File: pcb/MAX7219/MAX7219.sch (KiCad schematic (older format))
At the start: 17 parts, among them J1 Conn_01x02, J2 Conn_01x08, J3 Conn_01x06, SW1 SW_SPST, SW2 SW_SPST, SW3 SW_SPST, SW4 SW_SPST, SW5 SW_SPST, SW6 SW_SPST, SW7 SW_SPST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

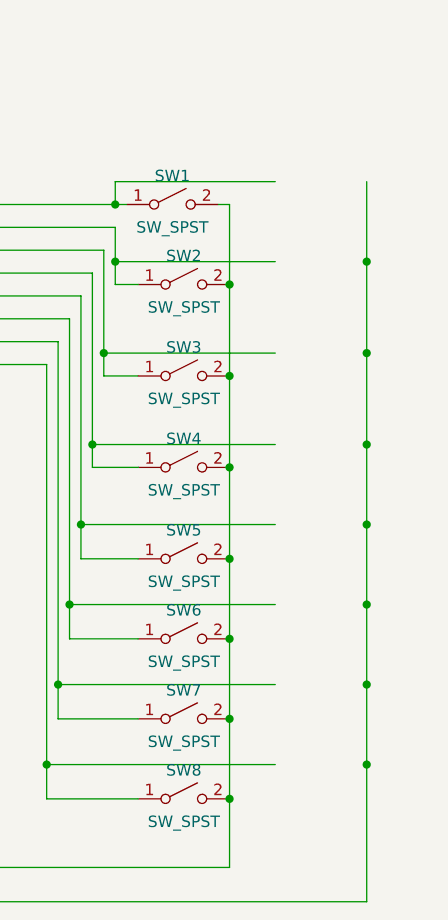
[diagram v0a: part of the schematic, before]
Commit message: Improved ioExpansion
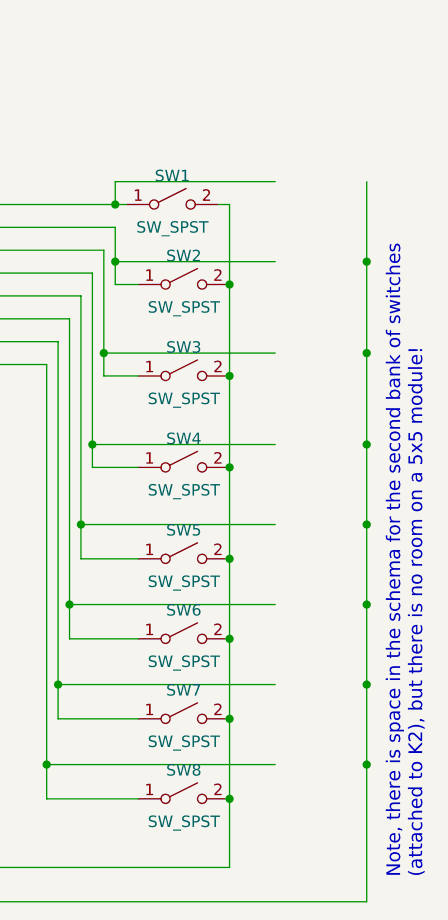
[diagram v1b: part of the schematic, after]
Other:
- note added: "Note, there is space in the schema for the second bank of switches\n(attached to K2), but there is no room on a 5x5 module!"
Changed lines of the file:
@@
 Text Label 4000 1600 2    60   ~ 0
 GND
+Text Notes 7400 4850 1    60   ~ 0
+Note, there is space in the schema for the second bank of switches\n(attached to K2), but there is no room on a 5x5 module!
 $EndSCHEMATC

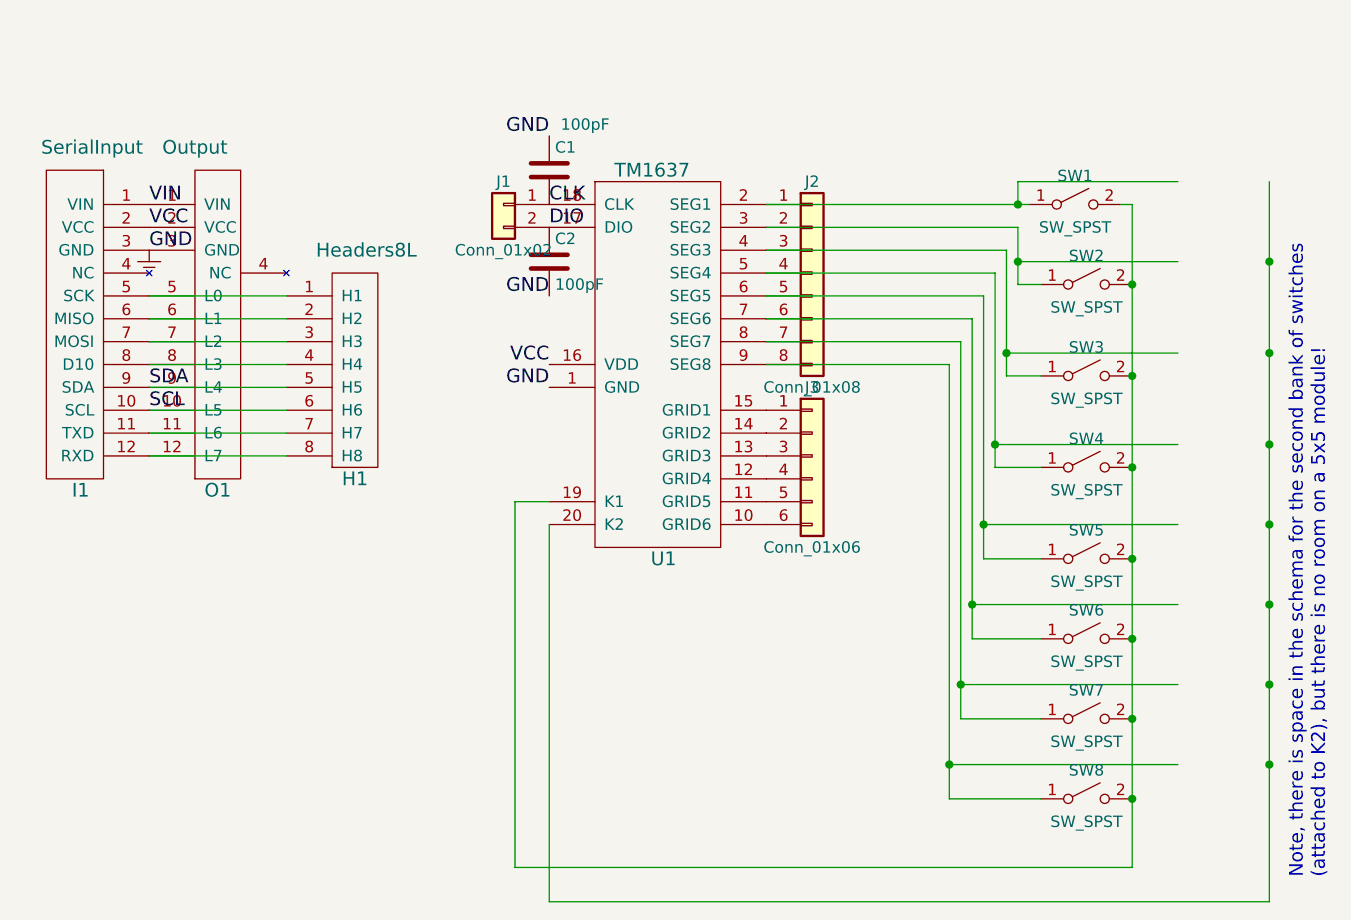
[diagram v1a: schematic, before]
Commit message: Added terminal connectors to the header pins half module. Tweaked the MAX7219 module, and added both common anode and common cathode to stripLED modules.
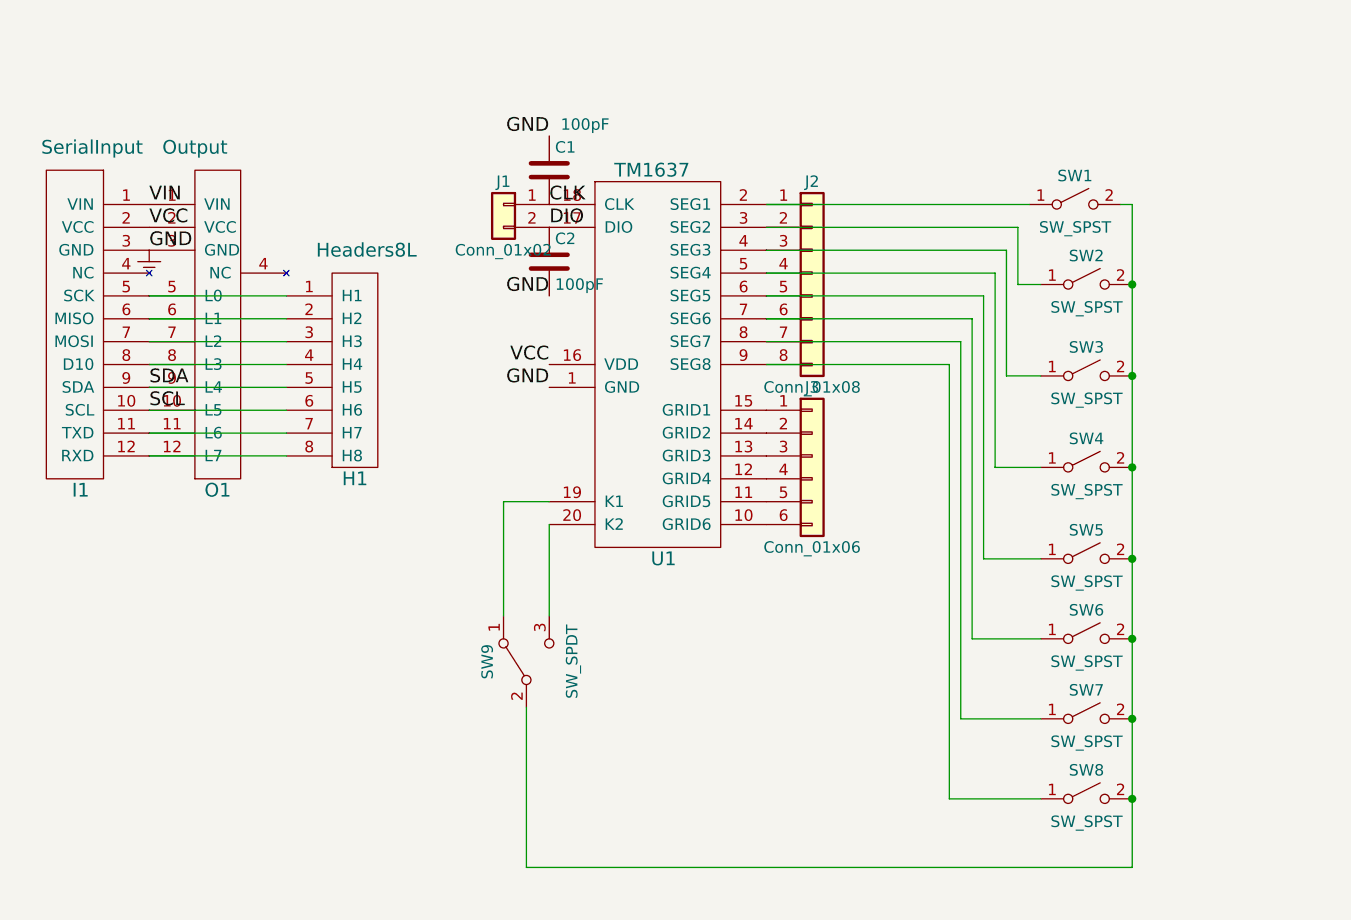
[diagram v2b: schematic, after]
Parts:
- added SW9: SW_SPDT, Buttons_Switches_THT:SW_CuK_JS202011CQN_DPDT_Straight, symbol SW_SPDT
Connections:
- wire segments 47 -> 37
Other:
- note removed: "Note, there is space in the schema for the second bank of switches\n(attached to K2), but there is no room on a 5x5 module!"
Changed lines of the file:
@@
 	5750 4500 6150 4500
 Wire Wire Line
-	4000 3200 3850 3200
+	3800 3200 4000 3200
 Wire Wire Line
-	3850 3200 3850 4800
+	6550 4800 3900 4800
 Wire Wire Line
-	3850 4800 6550 4800
-Wire Wire Line
-	6550 4800 6550 1900
+	6550 1900 6550 4800
 Connection ~ 6550 4150
 Connection ~ 6550 3800
@@
 	6550 1900 6500 1900
 Connection ~ 6550 4500
-Wire Wire Line
-	4000 3300 4000 4950
-Wire Wire Line
-	6050 1800 6750 1800
-Wire Wire Line
-	6050 1800 6050 1900
-Connection ~ 6050 1900
-Wire Wire Line
-	6750 2150 6050 2150
-Connection ~ 6050 2150
-Wire Wire Line
-	6750 2550 6000 2550
-Connection ~ 6000 2550
-Wire Wire Line
-	6750 2950 5950 2950
-Connection ~ 5950 2950
-Wire Wire Line
-	6750 3300 5900 3300
-Connection ~ 5900 3300
-Wire Wire Line
-	6750 3650 5850 3650
-Connection ~ 5850 3650
-Wire Wire Line
-	6750 4000 5800 4000
-Connection ~ 5800 4000
-Connection ~ 5750 4350
-Wire Wire Line
-	7150 1800 7150 4950
-Connection ~ 7150 2150
-Connection ~ 7150 2550
-Connection ~ 7150 2950
-Connection ~ 7150 3300
-Connection ~ 7150 3650
-Connection ~ 7150 4000
-Connection ~ 7150 4350
-Wire Wire Line
-	7150 4950 4000 4950
-Wire Wire Line
-	6750 4350 5750 4350
 Text Label 4000 1900 0    60   ~ 0
 CLK
@@
 Text Label 4000 1600 2    60   ~ 0
 GND
-Text Notes 7400 4850 1    60   ~ 0
-Note, there is space in the schema for the second bank of switches\n(attached to K2), but there is no room on a 5x5 module!
+$Comp
+L SW_SPDT SW9
+U 1 1 5AE7A76E
+P 3900 3900
+F 0 "SW9" H 3900 4070 50  0000 C CNN
+F 1 "SW_SPDT" H 3900 3700 50  0000 C CNN
+F 2 "Buttons_Switches_THT:SW_CuK_JS202011CQN_DPDT_Straight" H 3900 3900 50  0001 C CNN
+F 3 "" H 3900 3900 50  0001 C CNN
+	1    3900 3900
+	0    -1   -1   0
+$EndComp
+Wire Wire Line
+	3800 3700 3800 3200
+Wire Wire Line
+	4000 3300 4000 3700
+Wire Wire Line
+	3900 4800 3900 4100
 $EndSCHEMATC
